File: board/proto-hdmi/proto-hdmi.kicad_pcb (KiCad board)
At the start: 2 copper layers, 30.5 x 43.2 mm, 36 parts, among them J1 Conn_02x17_Odd_Even, J2 HDMI_A_1.4, J3 HDMI_A_1.4

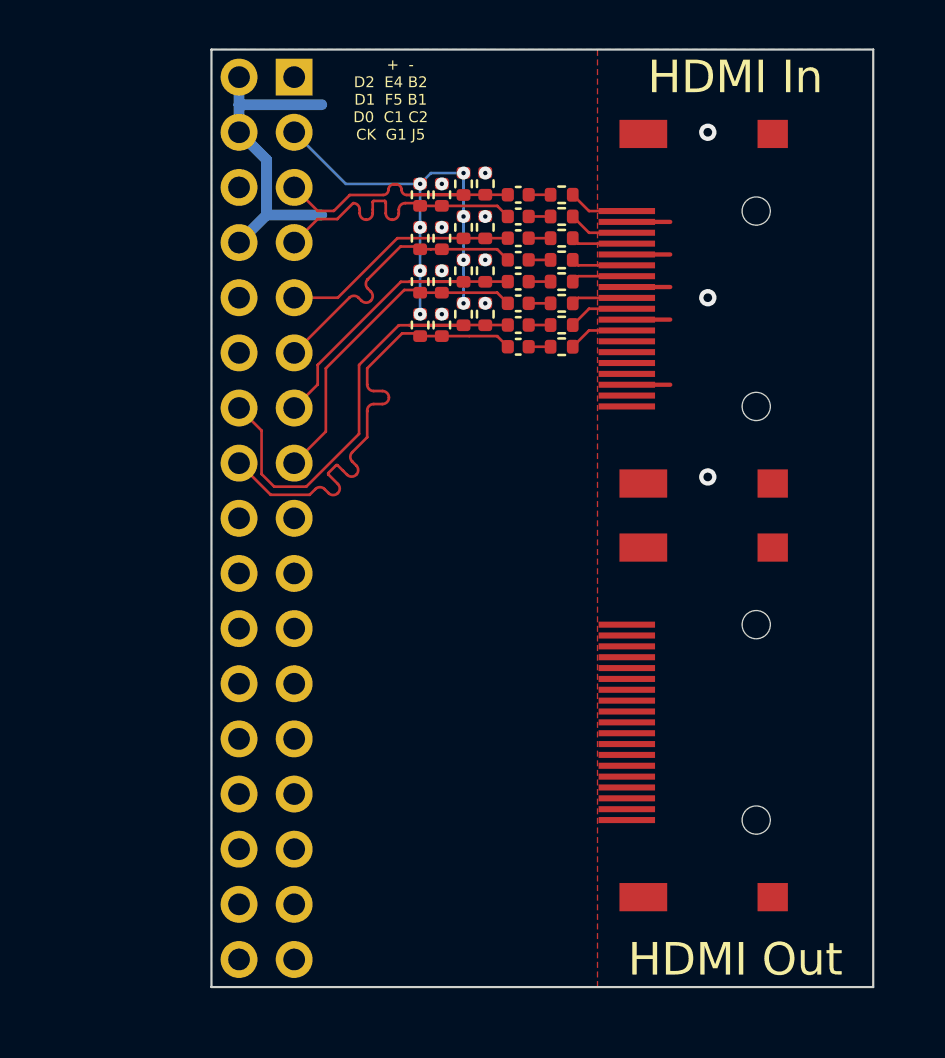
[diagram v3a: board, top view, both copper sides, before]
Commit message: Add and route non-TMDS lines for sink port.
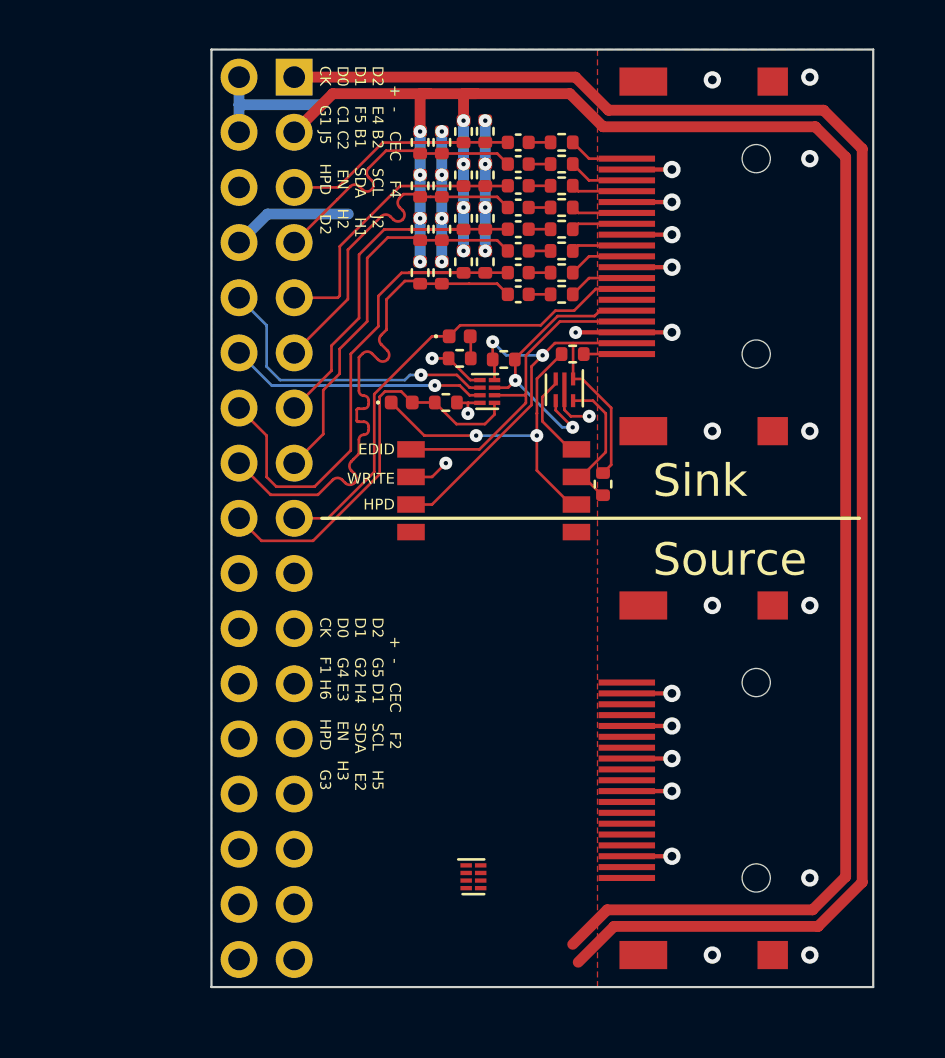
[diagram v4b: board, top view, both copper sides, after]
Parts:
- added D1: SBA0520Q, Diode_SMD:D_0402_1005Metric, F.Cu at (144.8, 103.4)
- added D2: SBA0520Q, Diode_SMD:D_0402_1005Metric, F.Cu at (142.1, 106.4)
- added R21: 27k, Resistor_SMD:R_0402_1005Metric, F.Cu at (144.8, 104.4)
- added R22: 10k, Resistor_SMD:R_0402_1005Metric, F.Cu at (144.1, 106.4)
- added R27: 47k, Resistor_SMD:R_0402_1005Metric, F.Cu at (146.8, 104.4)
- added R28: 10k, Resistor_SMD:R_0402_1005Metric, F.Cu at (151.4, 110.2)
- added R29: 1k, Resistor_SMD:R_0402_1005Metric, F.Cu at (150.0, 104.2)
- added SW1: CTS_218-4LPSTR, 0Local:CTS_218-4, F.Cu at (146.3, 110.5)
- added U1: NXP_NTS0302, Package_SON:X2SON-8_1.4x1mm_P0.35mm, F.Cu at (146.1, 105.9)
- added U2: NXP_NTS0302, Package_SON:X2SON-8_1.4x1mm_P0.35mm, F.Cu at (145.4, 128.3)
- added U3: M24C02, 0Local:ST_UFDFPN5, F.Cu at (149.6, 105.8)
- J2, J3: value HDMI_A_1.4 -> HDMI_A
- moved J3 2.67 mm to (152.5, 123.8)
- moved C1 2.41 mm to (147.5, 94.4)
- moved C2 2.41 mm to (147.5, 95.4)
- moved C3 2.41 mm to (147.5, 98.4)
- moved C4 2.41 mm to (147.5, 99.4)
- moved C5 2.41 mm to (147.5, 96.4)
- moved C6 2.41 mm to (147.5, 97.4)
- moved C7 2.41 mm to (147.5, 100.4)
- moved C8 2.41 mm to (147.5, 101.4)
- moved J2 2.41 mm to (152.5, 99.7)
- moved R1 2.41 mm to (149.5, 94.4)
- moved R10 2.41 mm to (146.0, 97.9)
- moved R11 2.41 mm to (145.0, 93.9)
- moved R12 2.41 mm to (145.0, 97.9)
- moved R13 2.41 mm to (144.0, 94.4)
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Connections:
- net /HDMI_CK_N renamed /HDMI In/HDMI_CK_N
- net /HDMI_CK_P renamed /HDMI In/HDMI_CK_P
- net /HDMI_D0_N renamed /HDMI In/HDMI_D0_N
- net /HDMI_D0_P renamed /HDMI In/HDMI_D0_P
- net /HDMI_D1_N renamed /HDMI In/HDMI_D1_N
- net /HDMI_D1_P renamed /HDMI In/HDMI_D1_P
- net /HDMI_D2_N renamed /HDMI In/HDMI_D2_N
- net /HDMI_D2_P renamed /HDMI In/HDMI_D2_P
- net /LVDS_CK_N renamed /IN_CK_N
- net /LVDS_CK_P renamed /IN_CK_P
- net /LVDS_D0_N renamed /IN_D0_N
- net /LVDS_D0_P renamed /IN_D0_P
- net /LVDS_D1_N renamed /IN_D1_N
- net /LVDS_D1_P renamed /IN_D1_P
- net /LVDS_D2_N renamed /IN_D2_N
- net /LVDS_D2_P renamed /IN_D2_P
- J1 pad 10: unconnected-(J1-Pad10) -> /IN_SCL
- J1 pad 12: unconnected-(J1-Pad12) -> /IN_SDA
- J1 pad 17: unconnected-(J1-Pad17) -> /IN_CEC
- J1 pad 18: unconnected-(J1-Pad18) -> /IN_ENABLE
- J1 pad 19: unconnected-(J1-Pad19) -> /IN_DETECT
- J1 pad 21: unconnected-(J1-Pad21) -> /OUT_D2_P
- J1 pad 22: unconnected-(J1-Pad22) -> /OUT_D1_P
- J1 pad 23: unconnected-(J1-Pad23) -> /OUT_D2_N
- J1 pad 24: unconnected-(J1-Pad24) -> /OUT_D1_N
- J1 pad 25: unconnected-(J1-Pad25) -> /OUT_D0_P
- J1 pad 26: unconnected-(J1-Pad26) -> /OUT_CK_P
- J1 pad 27: unconnected-(J1-Pad27) -> /OUT_D0_N
- J1 pad 28: unconnected-(J1-Pad28) -> /OUT_CK_N
- J1 pad 29: unconnected-(J1-Pad29) -> /OUT_SCL
- J1 pad 30: unconnected-(J1-Pad30) -> /OUT_CEC
- J1 pad 31: unconnected-(J1-Pad31) -> /OUT_SDA
- J1 pad 32: unconnected-(J1-Pad32) -> /OUT_ENABLE
- J1 pad 33: unconnected-(J1-Pad33) -> /OUT_DETECT
- J2 pad 13: unconnected-(J2-Pad13) -> /IN_CEC
- J2 pad 15: unconnected-(J2-Pad15) -> /HDMI In/HDMI_SCL
- J2 pad 16: unconnected-(J2-Pad16) -> /HDMI In/HDMI_SDA
- J2 pad 18: unconnected-(J2-Pad18) -> /HDMI In/HDMI_+5V
- J2 pad 19: unconnected-(J2-Pad19) -> /HDMI In/HDMI_HPD
- J3 pad 1: (no net) -> /HDMI Out/HDMI_D2_P
- J3 pad 10: (no net) -> /HDMI Out/HDMI_CK_P
- J3 pad 11: (no net) -> GND
- J3 pad 12: (no net) -> /HDMI Out/HDMI_CK_N
- J3 pad 13: (no net) -> /OUT_CEC
- J3 pad 14: (no net) -> unconnected-(J3-Pad14)
- J3 pad 15: (no net) -> /HDMI Out/HDMI_SCL
- J3 pad 16: (no net) -> /HDMI Out/HDMI_SDA
- J3 pad 17: (no net) -> GND
- J3 pad 18: (no net) -> /HDMI Out/HDMI_+5V
- J3 pad 19: (no net) -> /HDMI Out/HDMI_HPD
- J3 pad 2: (no net) -> GND
- J3 pad 3: (no net) -> /HDMI Out/HDMI_D2_N
- J3 pad 4: (no net) -> /HDMI Out/HDMI_D1_P
- J3 pad 5: (no net) -> GND
- J3 pad 6: (no net) -> /HDMI Out/HDMI_D1_N
- J3 pad 7: (no net) -> /HDMI Out/HDMI_D0_P
- J3 pad 8: (no net) -> GND
- J3 pad 9: (no net) -> /HDMI Out/HDMI_D0_N
- J3 pad SH: (no net) -> GND
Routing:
- net +5V: track 0.00 -> 75.9 mm
- net +3V3: track 21.1 -> 93.0 mm, vias 8 -> 9
- net GND: track 25.1 -> 52.8 mm, vias 11 -> 32
- net /HDMI In/HDMI_+5V: track 0.00 -> 25.5 mm, vias 0 -> 2
- net /IN_CEC: track 0.00 -> 21.8 mm
- net /IN_ENABLE: track 0.00 -> 18.5 mm
- net Net-(SW1-Pad6): track 0.00 -> 15.6 mm, vias 0 -> 2
- net /HDMI In/HDMI_SDA: track 0.00 -> 15.1 mm
- net /IN_SCL: track 0.00 -> 14.1 mm, vias 0 -> 1
- net /HDMI In/HDMI_SCL: track 0.00 -> 13.2 mm, vias 0 -> 2
- net /IN_SDA: track 0.00 -> 11.9 mm, vias 0 -> 1
- net /HDMI In/~{WC}: track 0.00 -> 6.92 mm
- net Net-(SW1-Pad8): track 0.00 -> 4.31 mm
- net /IN_D0_N: track 15.1 -> 18.0 mm
- net /IN_D0_P: track 15.3 -> 18.1 mm
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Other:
- board text added: "+ - CEC F2 D2 G5 D1 SCL H5 D1 G2 H4 SDA E2 D0 G4 E3 EN H3 CK F1 H6 HPD G3"
- board text added: "+ - CEC F4 D2 E4 B2 SCL J2 D1 F5 B1 SDA H1 D0 C1 C2 EN H2 CK G1 J5 HPD D2"
- board text added: "EDID"
- board text added: "HPD"
- board text added: "Sink"
- board text added: "Source"
- board text added: "WRITE"
- board text removed: "+ - D2 E4 B2 D1 F5 B1 D0 C1 C2 CK G1 J5"
- board text removed: "HDMI In"
- board text removed: "HDMI Out"

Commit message: Connect source port hotplug detect.
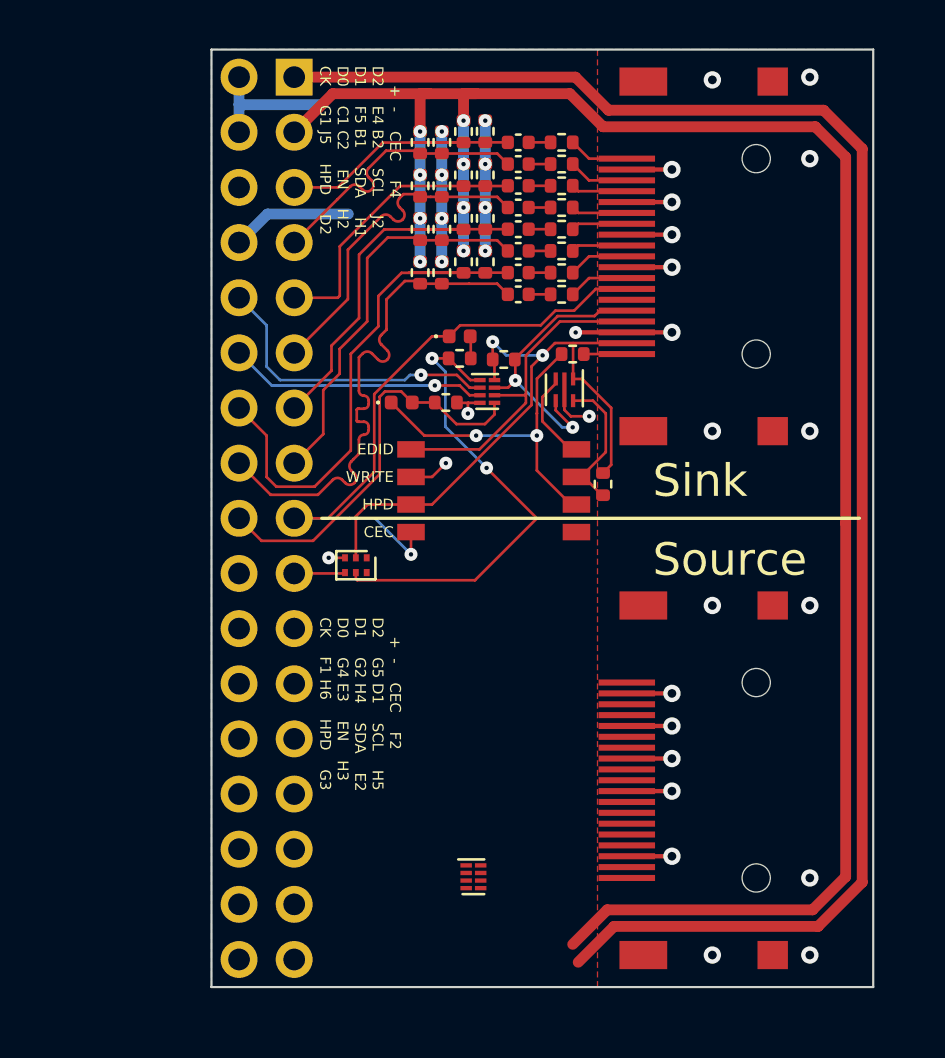
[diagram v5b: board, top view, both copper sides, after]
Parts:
- added U4: 74LVC1G17, Package_TO_SOT_SMD:SOT-886, F.Cu at (140.0, 113.9)
- U1: value NXP_NTS0302 -> NTS0302
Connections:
- net +3V3 renamed VCC
- SW1 pad 4: unconnected-(SW1-Pad4) -> /IN_CEC
- SW1 pad 5: unconnected-(SW1-Pad5) -> /OUT_CEC
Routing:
- net VCC: track 93.0 -> 126.5 mm, vias 9 -> 10
- net /IN_CEC: track 21.8 -> 28.9 mm, vias 0 -> 1
- net /HDMI In/HDMI_+5V: track 25.5 -> 30.2 mm
- net /IN_DETECT: track 0.00 -> 2.36 mm
- net GND: track 52.8 -> 53.5 mm, vias 32 -> 33
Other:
- board text added: "CEC"
